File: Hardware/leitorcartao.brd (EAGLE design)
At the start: 34.5 x 56.7 mm, 157 parts, among them IC1 TL084, IC2 TL084, Q1 BSH103, Q2 BC847ASMD, Q3 BC857ALT1SMD, Q4 BC847ALT1SMD, Q5 BC847ALT1SMD, Q6 BC847ALT1SMD, Q7 BC847ALT1SMD, U1 SAMD20E14A-AUT, U3 TLV1117-50CDCYR, U4 MFRC52202HN1, U5 LP2985-33DBVR, X1 ANTENA 125kHz, X2 MIFARE ANTENA

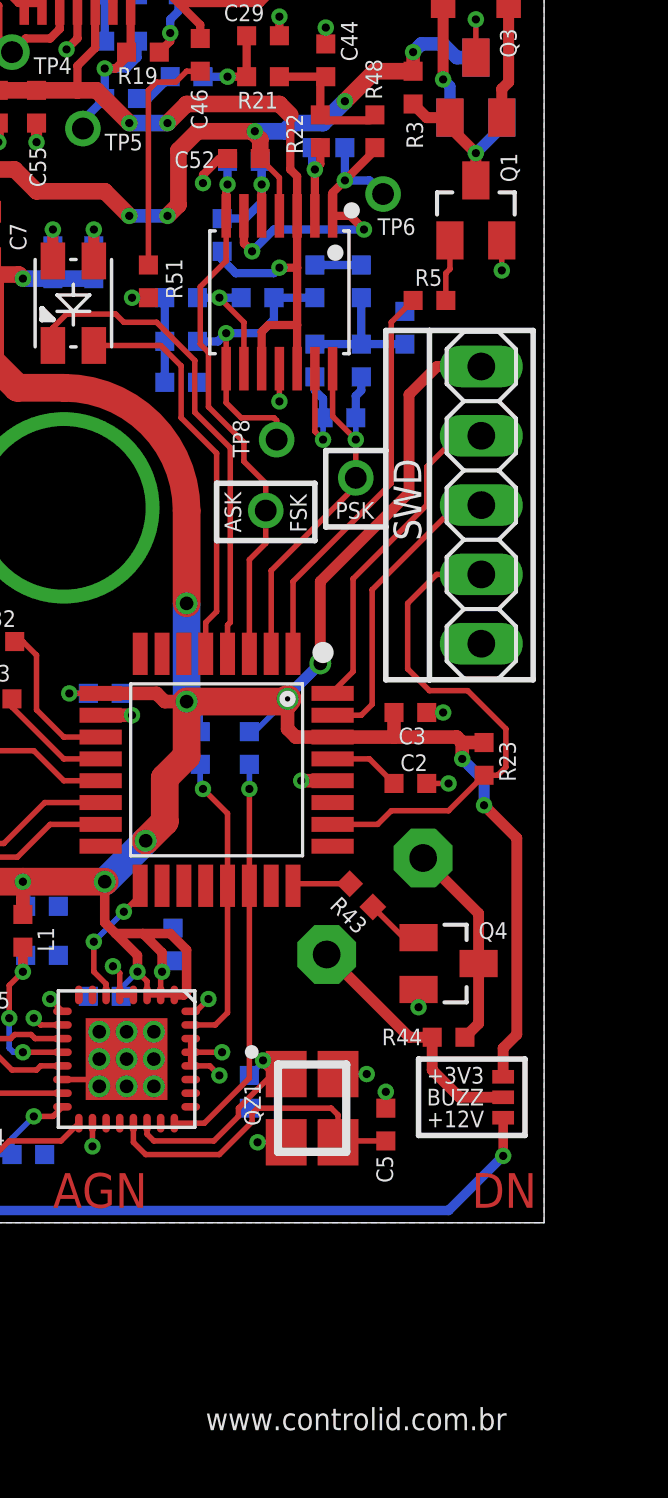
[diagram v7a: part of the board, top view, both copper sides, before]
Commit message: Alterações solicitadas por Albert. Aguradando David.
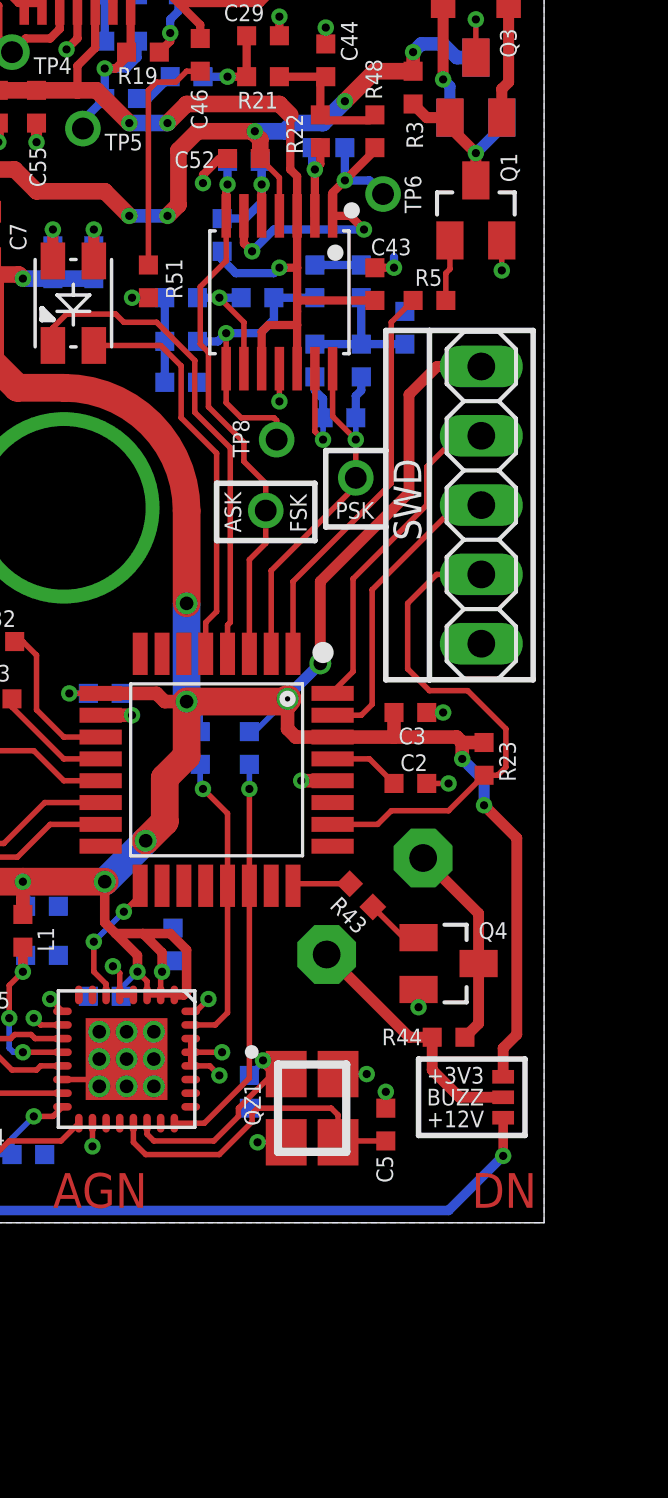
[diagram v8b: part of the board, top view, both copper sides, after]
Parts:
- added C43: 100nF, RFiD:C0402
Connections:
- net GND: now also C43.2
- net V+: now also C43.1
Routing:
- net V+: track 37.0 -> 39.9 mm
- net GND: track 54.1 -> 55.2 mm, vias 51 -> 52
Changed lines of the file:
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@@
 <grid distance="0.1" unitdist="mm" unit="mm" style="lines" multiple="1" display="yes" altdistance="0.05" altunitdist="mm" altunit="mm"/>
 <layers>
-<layer number="1" name="Top" color="4" fill="1" visible="yes" active="yes"/>
+<layer number="1" name="Top" color="4" fill="1" visible="no" active="yes"/>
 <layer number="2" name="Route2" color="1" fill="3" visible="no" active="no"/>
 <layer number="3" name="Route3" color="4" fill="3" visible="no" active="no"/>
@@
 <layer number="14" name="Route14" color="1" fill="6" visible="no" active="no"/>
 <layer number="15" name="Route15" color="4" fill="6" visible="no" active="no"/>
-<layer number="16" name="Bottom" color="1" fill="1" visible="no" active="yes"/>
+<layer number="16" name="Bottom" color="1" fill="1" visible="yes" active="yes"/>
 <layer number="17" name="Pads" color="2" fill="1" visible="yes" active="yes"/>
 <layer number="18" name="Vias" color="2" fill="1" visible="yes" active="yes"/>
 <layer number="19" name="Unrouted" color="6" fill="1" visible="yes" active="yes"/>
 <layer number="20" name="Dimension" color="15" fill="1" visible="yes" active="yes"/>
-<layer number="21" name="tPlace" color="7" fill="1" visible="yes" active="yes"/>
-<layer number="22" name="bPlace" color="7" fill="1" visible="no" active="yes"/>
-<layer number="23" name="tOrigins" color="15" fill="1" visible="yes" active="yes"/>
-<layer number="24" name="bOrigins" color="15" fill="1" visible="no" active="yes"/>
-<layer number="25" name="tNames" color="7" fill="1" visible="yes" active="yes"/>
-<layer number="26" name="bNames" color="7" fill="1" visible="no" active="yes"/>
+<layer number="21" name="tPlace" color="7" fill="1" visible="no" active="yes"/>
+<layer number="22" name="bPlace" color="7" fill="1" visible="yes" active="yes"/>
+<layer number="23" name="tOrigins" color="15" fill="1" visible="no" active="yes"/>
+<layer number="24" name="bOrigins" color="15" fill="1" visible="yes" active="yes"/>
+<layer number="25" name="tNames" color="7" fill="1" visible="no" active="yes"/>
+<layer number="26" name="bNames" color="7" fill="1" visible="yes" active="yes"/>
 <layer number="27" name="tValues" color="7" fill="1" visible="no" active="yes"/>
 <layer number="28" name="bValues" color="7" fill="1" visible="no" active="yes"/>
-<layer number="29" name="tStop" color="7" fill="3" visible="yes" active="yes"/>
-<layer number="30" name="bStop" color="7" fill="6" visible="no" active="yes"/>
+<layer number="29" name="tStop" color="7" fill="3" visible="no" active="yes"/>
+<layer number="30" name="bStop" color="7" fill="6" visible="yes" active="yes"/>
 <layer number="31" name="tCream" color="7" fill="4" visible="no" active="yes"/>
 <layer number="32" name="bCream" color="7" fill="5" visible="no" active="yes"/>
@@
 <layer number="40" name="bKeepout" color="1" fill="11" visible="no" active="yes"/>
 <layer number="41" name="tRestrict" color="4" fill="10" visible="no" active="yes"/>
-<layer number="42" name="bRestrict" color="1" fill="10" visible="no" active="yes"/>
+<layer number="42" name="bRestrict" color="1" fill="10" visible="yes" active="yes"/>
 <layer number="43" name="vRestrict" color="2" fill="10" visible="no" active="yes"/>
 <layer number="44" name="Drills" color="7" fill="1" visible="no" active="yes"/>
@@
 <layer number="49" name="Reference" color="7" fill="1" visible="yes" active="yes"/>
 <layer number="50" name="dxf" color="7" fill="1" visible="no" active="no"/>
-<layer number="51" name="tDocu" color="7" fill="1" visible="yes" active="yes"/>
-<layer number="52" name="bDocu" color="7" fill="1" visible="no" active="yes"/>
+<layer number="51" name="tDocu" color="7" fill="1" visible="no" active="yes"/>
+<layer number="52" name="bDocu" color="7" fill="1" visible="yes" active="yes"/>
 <layer number="53" name="tGND_GNDA" color="7" fill="9" visible="no" active="no"/>
 <layer number="54" name="bGND_GNDA" color="1" fill="9" visible="no" active="no"/>
@@
 <wire x1="16.5" y1="33.1" x2="16.1" y2="33.1" width="0.2032" layer="21"/>
 <wire x1="16.1" y1="33.1" x2="16.2" y2="33.2" width="0.2032" layer="21"/>
-<text x="22.1" y="-7.6" size="0.8128" layer="21" font="vector" ratio="12">www.controlid.com.br</text>
 <text x="19.4" y="1.5" size="0.8128" layer="22" font="vector" ratio="12" rot="MR180">www.controlid.com.br</text>
 <text x="13.8" y="45.5" size="0.8128" layer="22" font="vector" ratio="12" rot="MR270">www.controlid.com.br</text>
@@
 <wire x1="22.5" y1="27.1" x2="26.1" y2="27.1" width="0.2032" layer="21"/>
 <wire x1="26.1" y1="27.1" x2="26.1" y2="25" width="0.2032" layer="21"/>
+<rectangle x1="17.9" y1="53.9" x2="18.2" y2="56.5" layer="42"/>
+<rectangle x1="29.9" y1="32.2" x2="34.4" y2="32.4" layer="42"/>
 </plain>
 <attributes>
@@
 <attribute name="MF" value="MOLEX" x="3.4" y="5.7" size="1.778" layer="28" rot="MR270" display="off"/>
 <attribute name="OC_FARNELL" value="1462926" x="3.4" y="5.7" size="1.778" layer="28" rot="MR270" display="off"/>
-<attribute name="NAME" x="1.49" y="6.24" size="0.6096" layer="26" font="vector" ratio="11" rot="MR270"/>
+<attribute name="NAME" x="2.66" y="2.79" size="0.6096" layer="26" font="vector" ratio="11" rot="MR180"/>
 <attribute name="VALUE" x="8.48" y="8.24" size="1" layer="28" ratio="14" rot="MR270"/>
 <attribute name="CUSTOMER_PN" value="-" x="3.4" y="5.7" size="1.778" layer="28" rot="MR270" display="off"/>
@@
 </element>
 <element name="TP6" library="RFiD" package="TESTPOINT" value="TESTPOINT" x="28.6" y="37.7" smashed="yes">
-<attribute name="NAME" x="28.4" y="36.2" size="0.6096" layer="25" font="vector" ratio="11"/>
+<attribute name="NAME" x="30" y="37" size="0.6096" layer="25" font="vector" ratio="11" rot="R90"/>
 <attribute name="VALUE" x="27.7" y="36.2" size="1" layer="27" font="vector" ratio="11"/>
 </element>
@@
 </element>
 <element name="SJ?1" library="RFiD" package="SOLDERBRIDGE" value="SOLDERBRIDGE" x="33" y="4.6" rot="R180"/>
+<element name="C43" library="RFiD" package="C0402" value="100nF" x="28.3" y="34.4" smashed="yes" rot="R90">
+<attribute name="NAME" x="29.635" y="36.065" size="0.6096" layer="25" font="vector" ratio="11" rot="R180"/>
+<attribute name="VALUE" x="30.205" y="33.765" size="1.27" layer="27" rot="R90"/>
+</element>
 </elements>
 <signals>
@@
 <via x="28.7" y="4.8" extent="1-16" drill="0.3"/>
 <wire x1="18.95" y1="8.35" x2="19.45" y2="8.35" width="0.2032" layer="1"/>
+<contactref element="C43" pad="2"/>
+<wire x1="28.3" y1="35" x2="29" y2="35" width="0.3048" layer="1"/>
+<via x="29" y="35" extent="1-16" drill="0.3"/>
+<wire x1="29" y1="35" x2="29" y2="35.4" width="0.3048" layer="16"/>
 </signal>
 <signal name="+3V3">
@@
 <contactref element="IC2" pad="10"/>
 <contactref element="R50" pad="2"/>
-<wire x1="25.45" y1="34.996334375" x2="25.45" y2="32.9" width="0.3048" layer="1"/>
+<wire x1="25.45" y1="34.996334375" x2="25.45" y2="33.8" width="0.3048" layer="1"/>
+<wire x1="25.45" y1="33.4" x2="25.45" y2="32.9" width="0.3048" layer="1"/>
 <wire x1="24.15" y1="32.65" x2="24.4" y2="32.9" width="0.3048" layer="1"/>
 <wire x1="24.4" y1="32.9" x2="25.45" y2="32.9" width="0.3048" layer="1"/>
@@
 <wire x1="13.9" y1="41.5" x2="13.5" y2="41.9" width="0.6096" layer="1"/>
 <wire x1="13.5" y1="41.9" x2="13.5" y2="42.5" width="0.6096" layer="1"/>
+<contactref element="C43" pad="1"/>
+<wire x1="28.3" y1="33.8" x2="25.45" y2="33.8" width="0.3048" layer="1"/>
+<wire x1="25.45" y1="33.8" x2="25.45" y2="33.4" width="0.3048" layer="1"/>
 </signal>
 <signal name="N$77">
